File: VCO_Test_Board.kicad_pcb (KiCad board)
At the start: 2 copper layers, 99.1 x 71.1 mm, 19 parts, among them J1 PCB.SMAFRA.HT, J2 PCB.SMAFRA.HT, J3 Tune Voltage Input, J4 VCC, Y1 MAX2607EUT+T

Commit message: Export gerber files.
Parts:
- moved C5 69.3 mm to (95.0, 59.7)
- moved L2 69.0 mm to (48.3, 49.5)
- moved L3 69.0 mm to (54.3, 50.3)
- moved C1 69.0 mm to (54.3, 56.1)
- moved C3 69.0 mm to (77.7, 56.0)
- moved C4 69.0 mm to (95.0, 51.0)
- moved J2 69.0 mm to (109.2, 79.3)
- moved J3 69.0 mm to (40.6, 78.9)
- moved J4 69.0 mm to (111.8, 56.0)
- moved L1 69.0 mm to (51.9, 45.9)
- moved L4 69.0 mm to (66.0, 48.7)
- moved L5 69.0 mm to (66.0, 54.4)
- moved R1 69.0 mm to (44.7, 57.9)
- moved R2 69.0 mm to (69.5, 54.4)
- moved R3 69.0 mm to (69.5, 48.7)
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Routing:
- net GND: track 22.9 -> 20.4 mm
- net Net-(J4-Pin_1): track 21.0 -> 19.0 mm
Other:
- board size 99.1 x 71.1 mm -> 101.6 x 67.7 mm

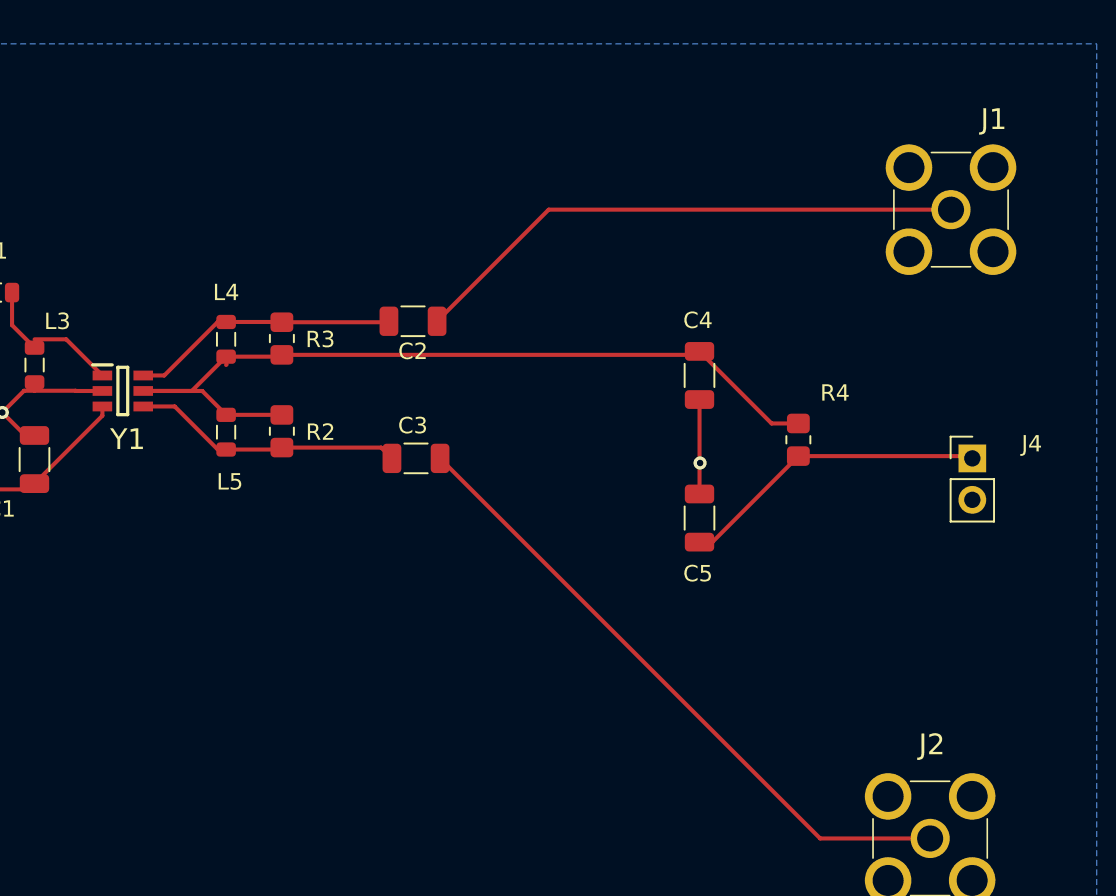
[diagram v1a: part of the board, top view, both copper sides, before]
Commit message: Swap out C5 for Tantalum capacitor. Final export for board order.
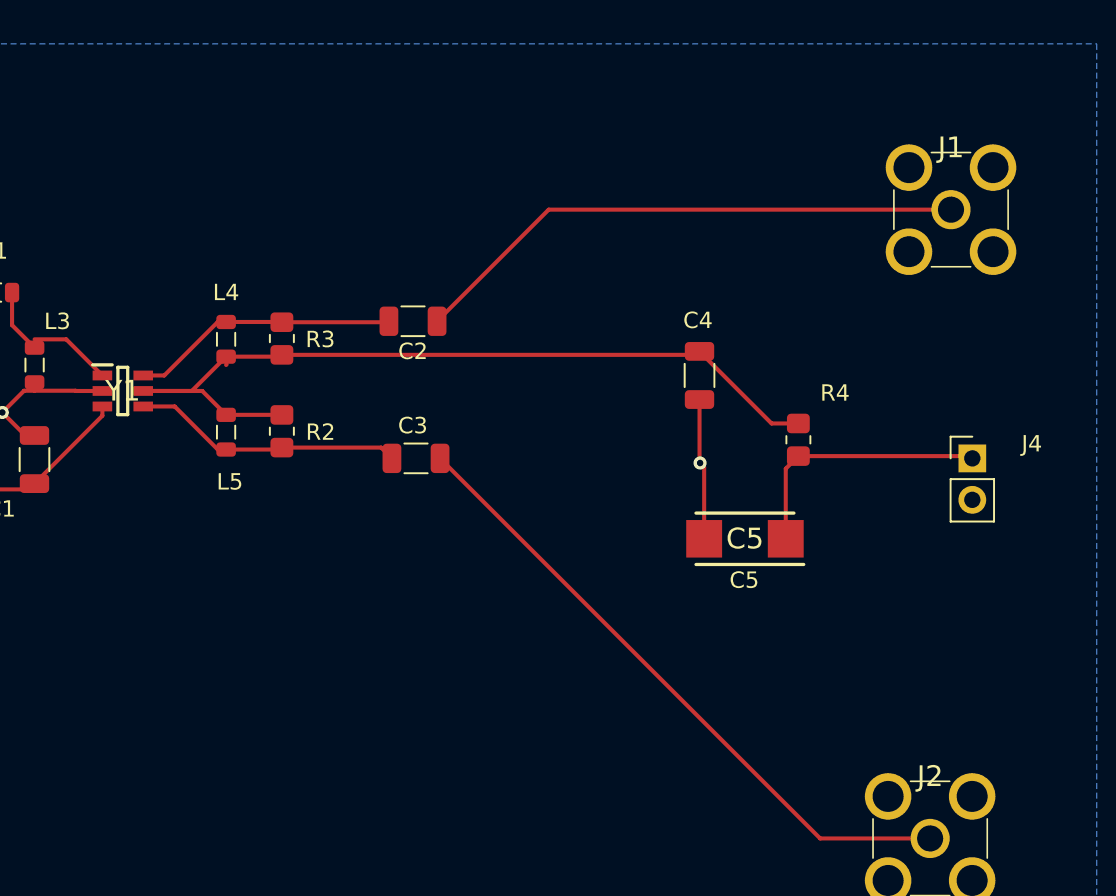
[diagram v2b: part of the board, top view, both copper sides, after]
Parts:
- C5: footprint Capacitor_SMD:C_1206_3216Metric -> Mouser:CAPPM6032X280N
- moved C5 3.06 mm to (97.8, 61.0), turned to 180 degrees
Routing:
- net GND: track 20.4 -> 23.3 mm
- net Net-(C5-+): track 19.0 -> 16.1 mm
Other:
- board text added: "10 uF"
- board text added: "C5"

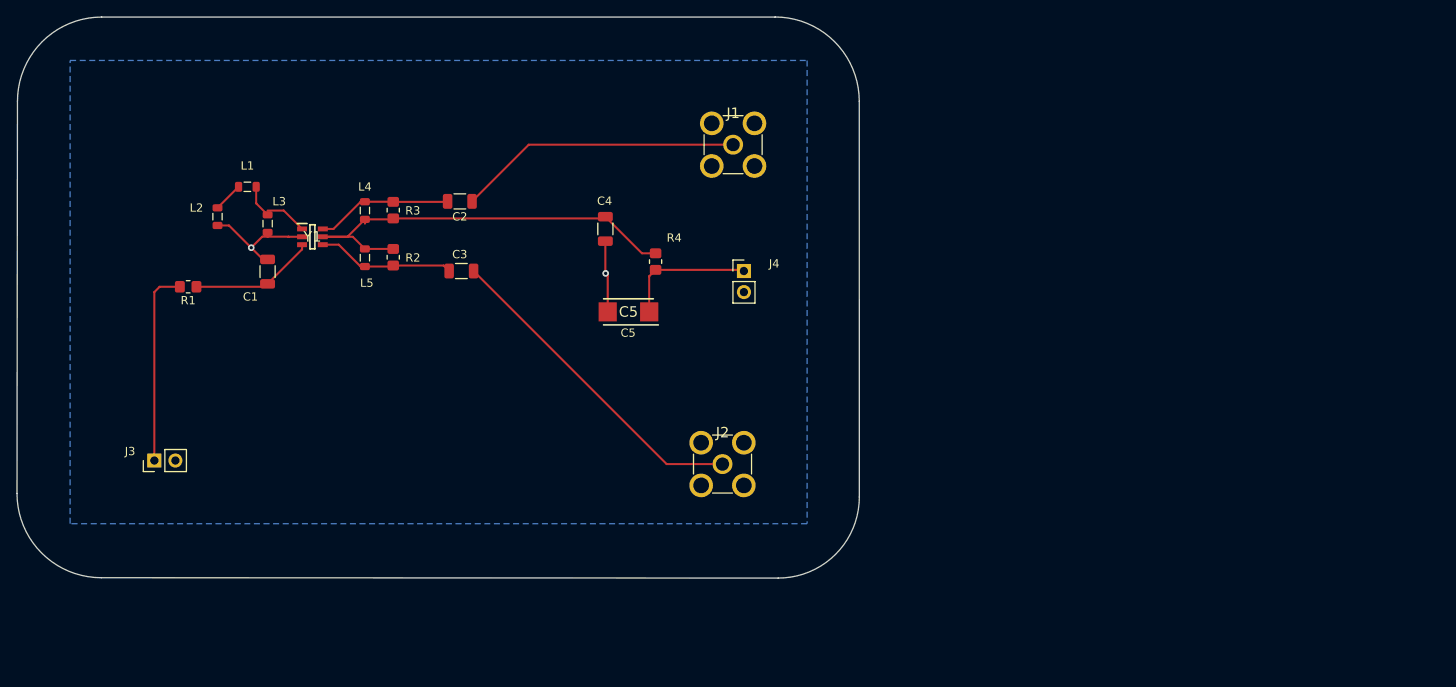
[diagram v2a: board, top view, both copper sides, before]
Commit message: Add mounting holes. Fix silkscreen in a few places.
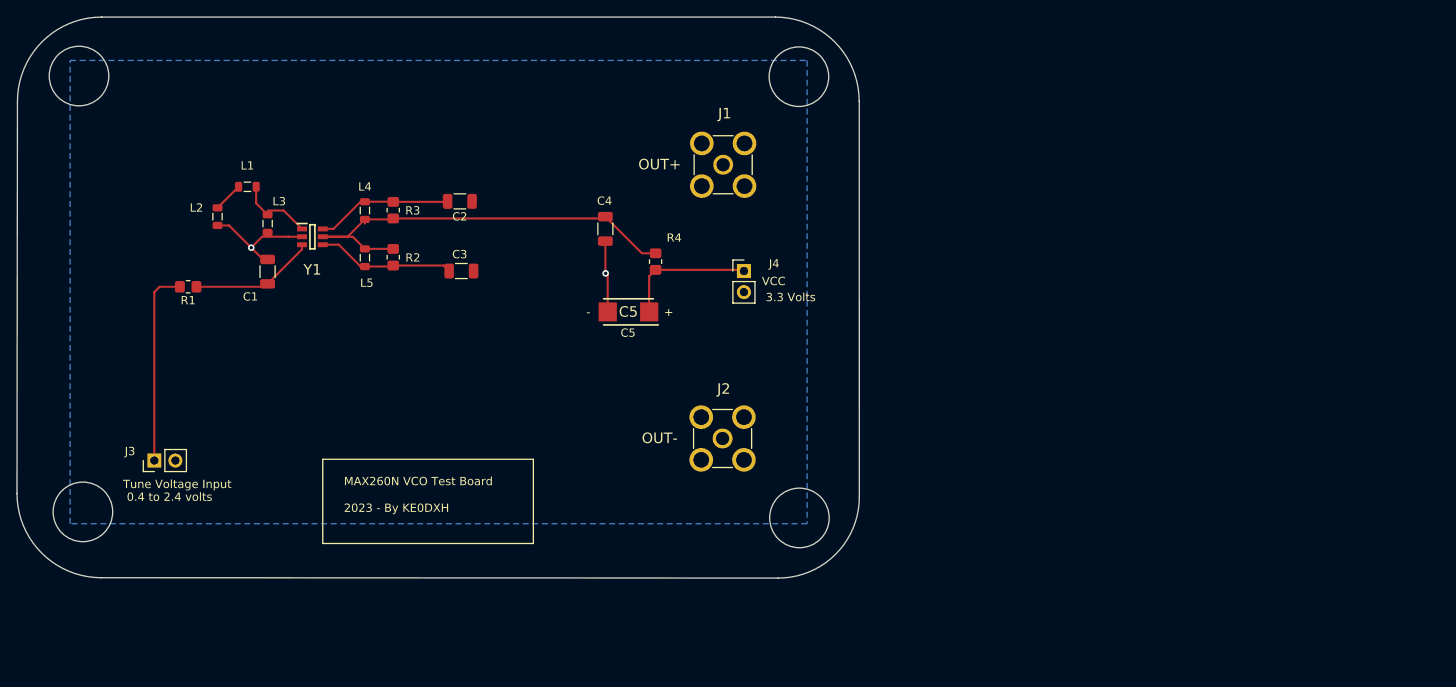
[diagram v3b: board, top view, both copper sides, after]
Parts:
- moved J2 3.09 mm to (109.2, 76.2), turned to -90 degrees
- moved J1 2.70 mm to (109.3, 43.2), turned to -90 degrees
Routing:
- net Net-(C3-Pad1): track 39.7 -> 0.00 mm
- net Net-(C2-Pad1): track 33.1 -> 0.00 mm
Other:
- outline, holes or cut-outs redrawn
- board text added: "+"
- board text added: "-"
- board text added: "MAX260N VCO Test Board 2023 - By KE0DXH"
- board text added: "OUT+"
- board text added: "OUT-"
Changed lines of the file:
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@@
     (property "ki_description" "MAXIM INTEGRATED PRODUCTS - MAX2607EUT+T - VCO, DIFF OUTPUT, 300MHZ, 5.5V, SOT-23")
     (attr smd)
-    (fp_text reference "Y1" (at 0 0) (layer "F.SilkS")
+    (fp_text reference "Y1" (at 0 3.975923) (layer "F.SilkS")
         (effects (font (size 1.27 1.27) (thickness 0.254)))
     )
@@
         (effects (font (size 1 1) (thickness 0.15)))
     )
-    (fp_text value "Tune Voltage Input" (at -2.85678 2.774945) (layer "F.Fab")
+    (fp_text value "Tune Voltage Input" (at -2.85678 2.774945) (layer "F.SilkS")
         (effects (font (size 1 1) (thickness 0.15)))
     )
@@
   )
   (footprint "Mouser:PCBSMAFRAHT" (layer "F.Cu")
-    (at 110.455 40.794077)
+    (at 109.255 43.215 -90)
     (descr "PCB.SMAFRA.HT-2")
     (tags "Connector")
@@
     (property "ki_description" "RF Connectors / Coaxial Connectors SMA RA PCB Mount, Jack, Gold, 50 , Through Hole Pin")
     (attr through_hole)
-    (fp_text reference "J1" (at 0 -3.8) (layer "F.SilkS")
+    (fp_text reference "J1" (at -6.179724 -0.190511) (layer "F.SilkS")
         (effects (font (size 1.27 1.27) (thickness 0.254)))
     )
-    (fp_text value "PCB.SMAFRA.HT" (at 0 -3.8) (layer "F.SilkS") hide
-        (effects (font (size 1.27 1.27) (thickness 0.254)))
-    )
-    (fp_text user "${REFERENCE}" (at 0 -3.8) (layer "F.Fab")
+    (fp_text value "PCB.SMAFRA.HT" (at 0 -3.8 90) (layer "F.SilkS") hide
         (effects (font (size 1.27 1.27) (thickness 0.254)))
     )
@@
     (fp_line (start 3.5 3.5) (end -3.5 3.5)
       (stroke (width 0.2) (type solid)) (layer "F.Fab"))
-    (pad "1" thru_hole circle (at 0 0) (size 2.4 2.4) (drill 1.6) (layers "*.Cu" "*.Mask")
+    (pad "1" thru_hole circle (at 0 0 270) (size 2.4 2.4) (drill 1.6) (layers "*.Cu" "*.Mask")
       (net 3 "Net-(C2-Pad1)") (pinfunction "1") (pintype "passive"))
-    (pad "2" thru_hole circle (at -2.575 -2.575) (size 2.85 2.85) (drill 1.9) (layers "*.Cu" "*.Mask")
+    (pad "2" thru_hole circle (at -2.575 -2.575 270) (size 2.85 2.85) (drill 1.9) (layers "*.Cu" "*.Mask")
       (net 2 "GND") (pinfunction "2") (pintype "passive"))
-    (pad "3" thru_hole circle (at -2.575 2.575) (size 2.85 2.85) (drill 1.9) (layers "*.Cu" "*.Mask")
+    (pad "3" thru_hole circle (at -2.575 2.575 270) (size 2.85 2.85) (drill 1.9) (layers "*.Cu" "*.Mask")
       (net 2 "GND") (pinfunction "3") (pintype "passive"))
-    (pad "4" thru_hole circle (at 2.575 2.575) (size 2.85 2.85) (drill 1.9) (layers "*.Cu" "*.Mask")
+    (pad "4" thru_hole circle (at 2.575 2.575 270) (size 2.85 2.85) (drill 1.9) (layers "*.Cu" "*.Mask")
       (net 2 "GND") (pinfunction "4") (pintype "passive"))
-    (pad "5" thru_hole circle (at 2.575 -2.575) (size 2.85 2.85) (drill 1.9) (layers "*.Cu" "*.Mask")
+    (pad "5" thru_hole circle (at 2.575 -2.575 270) (size 2.85 2.85) (drill 1.9) (layers "*.Cu" "*.Mask")
       (net 2 "GND") (pinfunction "5") (pintype "passive"))
     (model "C:\\Users\\steve\\OneDrive\\Documents\\EDA\\SamacSys_Parts.3dshapes\\PCB.SMAFRA.HT.stp"
@@
         (effects (font (size 1 1) (thickness 0.15)))
     )
-    (fp_text value "VCC" (at 3.594817 1.237918) (layer "F.Fab")
+    (fp_text value "VCC" (at 3.594817 1.237918) (layer "F.SilkS")
         (effects (font (size 1 1) (thickness 0.15)))
     )
@@
   )
   (footprint "Mouser:PCBSMAFRAHT" (layer "F.Cu")
-    (at 109.175699 79.32015)
+    (at 109.185 76.235 -90)
     (descr "PCB.SMAFRA.HT-2")
     (tags "Connector")
@@
     (property "ki_description" "RF Connectors / Coaxial Connectors SMA RA PCB Mount, Jack, Gold, 50 , Through Hole Pin")
     (attr through_hole)
-    (fp_text reference "J2" (at 0 -3.8) (layer "F.SilkS")
+    (fp_text reference "J2" (at -5.975188 -0.144266) (layer "F.SilkS")
         (effects (font (size 1.27 1.27) (thickness 0.254)))
     )
-    (fp_text value "PCB.SMAFRA.HT" (at 0 -3.8) (layer "F.SilkS") hide
-        (effects (font (size 1.27 1.27) (thickness 0.254)))
-    )
-    (fp_text user "${REFERENCE}" (at 0 -3.8) (layer "F.Fab")
+    (fp_text value "PCB.SMAFRA.HT" (at 0 -3.8 90) (layer "F.SilkS") hide
         (effects (font (size 1.27 1.27) (thickness 0.254)))
     )
@@
     (fp_line (start 3.5 3.5) (end -3.5 3.5)
       (stroke (width 0.2) (type solid)) (layer "F.Fab"))
-    (pad "1" thru_hole circle (at 0 0) (size 2.4 2.4) (drill 1.6) (layers "*.Cu" "*.Mask")
+    (pad "1" thru_hole circle (at 0 0 270) (size 2.4 2.4) (drill 1.6) (layers "*.Cu" "*.Mask")
       (net 4 "Net-(C3-Pad1)") (pinfunction "1") (pintype "passive"))
-    (pad "2" thru_hole circle (at -2.575 -2.575) (size 2.85 2.85) (drill 1.9) (layers "*.Cu" "*.Mask")
+    (pad "2" thru_hole circle (at -2.575 -2.575 270) (size 2.85 2.85) (drill 1.9) (layers "*.Cu" "*.Mask")
       (net 2 "GND") (pinfunction "2") (pintype "passive"))
-    (pad "3" thru_hole circle (at -2.575 2.575) (size 2.85 2.85) (drill 1.9) (layers "*.Cu" "*.Mask")
+    (pad "3" thru_hole circle (at -2.575 2.575 270) (size 2.85 2.85) (drill 1.9) (layers "*.Cu" "*.Mask")
       (net 2 "GND") (pinfunction "3") (pintype "passive"))
-    (pad "4" thru_hole circle (at 2.575 2.575) (size 2.85 2.85) (drill 1.9) (layers "*.Cu" "*.Mask")
+    (pad "4" thru_hole circle (at 2.575 2.575 270) (size 2.85 2.85) (drill 1.9) (layers "*.Cu" "*.Mask")
       (net 2 "GND") (pinfunction "4") (pintype "passive"))
-    (pad "5" thru_hole circle (at 2.575 -2.575) (size 2.85 2.85) (drill 1.9) (layers "*.Cu" "*.Mask")
+    (pad "5" thru_hole circle (at 2.575 -2.575 270) (size 2.85 2.85) (drill 1.9) (layers "*.Cu" "*.Mask")
       (net 2 "GND") (pinfunction "5") (pintype "passive"))
     (model "C:\\Users\\steve\\OneDrive\\Documents\\EDA\\SamacSys_Parts.3dshapes\\PCB.SMAFRA.HT.stp"
@@
     )
   )
-  (gr_arc (start 115.510574 25.391716) (mid 122.694779 28.367511) (end 125.670574 35.551716)
+  (gr_rect (start 60.96 78.74) (end 86.36 88.9)
+    (stroke (width 0.15) (type default)) (fill none) (layer "F.SilkS"))
+  (gr_arc (start 115.57 25.400001) (mid 122.710034 28.394279) (end 125.662473 35.551716)
     (stroke (width 0.1) (type default)) (layer "Edge.Cuts"))
   (gr_line (start 34.233463 93.02852) (end 115.89509 93.071952)
@@
   (gr_line (start 125.681091 83.285951) (end 125.670574 35.551716)
     (stroke (width 0.1) (type default)) (layer "Edge.Cuts"))
+  (gr_circle (center 118.393006 32.593365) (end 121.985108 32.593365)
+    (stroke (width 0.15) (type default)) (fill none) (layer "Edge.Cuts"))
   (gr_arc (start 24.13 35.56) (mid 27.105795 28.375795) (end 34.29 25.4)
     (stroke (width 0.1) (type default)) (layer "Edge.Cuts"))
+  (gr_circle (center 31.555692 32.515133) (end 35.147794 32.515133)
+    (stroke (width 0.15) (type default)) (fill none) (layer "Edge.Cuts"))
   (gr_line (start 24.073463 82.86852) (end 24.13 35.56)
     (stroke (width 0.1) (type default)) (layer "Edge.Cuts"))
+  (gr_circle (center 32.025083 85.086912) (end 35.617185 85.086912)
+    (stroke (width 0.15) (type default)) (fill none) (layer "Edge.Cuts"))
   (gr_arc (start 34.233463 93.02852) (mid 27.049258 90.052725) (end 24.073463 82.86852)
     (stroke (width 0.1) (type default)) (layer "Edge.Cuts"))
   (gr_line (start 34.29 25.4) (end 115.57 25.4)
     (stroke (width 0.1) (type default)) (layer "Edge.Cuts"))
+  (gr_circle (center 118.453511 85.815264) (end 122.045613 85.815264)
+    (stroke (width 0.15) (type default)) (fill none) (layer "Edge.Cuts"))
+  (gr_text "OUT+" (at 101.6 43.18) (layer "F.SilkS")
+    (effects (font (size 1.27 1.27) (thickness 0.254)))
+  )
+  (gr_text "3.3 Volts" (at 117.404217 59.206251) (layer "F.SilkS")
+    (effects (font (size 1 1) (thickness 0.15)))
+  )
+  (gr_text "MAX260N VCO Test Board\n\n2023 - By KE0DXH\n\n" (at 63.5 83.82) (layer "F.SilkS")
+    (effects (font (size 1 1) (thickness 0.15)) (justify left))
+  )
+  (gr_text "0.4 to 2.4 volts" (at 42.477964 83.294119) (layer "F.SilkS")
+    (effects (font (size 1 1) (thickness 0.15)))
+  )
   (gr_text "C5" (at 97.79 63.5) (layer "F.SilkS")
     (effects (font (size 1 1) (thickness 0.15)))
   )
-  (gr_text "3.3 Volts" (at 117.404217 59.206251) (layer "F.Fab")
+  (gr_text "OUT-" (at 101.6 76.2) (layer "F.SilkS")
+    (effects (font (size 1.27 1.27) (thickness 0.254)))
+  )
+  (gr_text "+" (at 102.684462 61.004013) (layer "F.SilkS")
     (effects (font (size 1 1) (thickness 0.15)))
   )
-  (gr_text "0.4 to 2.4 volts" (at 42.477964 83.294119) (layer "F.Fab")
+  (gr_text "-" (at 92.986943 60.985819) (layer "F.SilkS")
     (effects (font (size 1 1) (thickness 0.15)))
   )
@@
   (via (at 95.079572 56.317657) (size 0.8) (drill 0.4) (layers "F.Cu" "B.Cu") (free) (net 2))
   (via (at 52.328723 53.221381) (size 0.8) (drill 0.4) (layers "F.Cu" "B.Cu") (free) (net 2))
-  (segment (start 78.966105 47.632526) (end 85.804554 40.794077) (width 0.25) (layer "F.Cu") (net 3))
-  (segment (start 85.804554 40.794077) (end 109.22 40.794077) (width 0.25) (layer "F.Cu") (net 3))
-  (segment (start 79.15 56.034077) (end 102.436073 79.32015) (width 0.25) (layer "F.Cu") (net 4))
-  (segment (start 102.436073 79.32015) (end 109.175699 79.32015) (width 0.25) (layer "F.Cu") (net 4))
   (segment (start 53.946097 57.934077) (end 54.299589 57.580585) (width 0.25) (layer "F.Cu") (net 5))
   (segment (start 45.72 57.934077) (end 53.946097 57.934077) (width 0.25) (layer "F.Cu") (net 5))
@@
     )
   )
-  (group "" (id 96585ef3-8c30-40ad-8ac0-88ff5b5410ec)
-    (members
-      2b9131db-60c4-4bd3-917c-fc71bccf163e
-      3e48a34a-59ec-4646-84b5-7698e987e1a7
-      70b12d8d-1f4b-4498-bade-dfc615c9c443
-      7de7da3b-8ee1-44ad-a89d-f5796a0eff8b
-      97735e73-0923-433e-8450-2501ef96361e
-      a1db13d8-aa48-4faa-ad8d-5f91cbae564e
-      b593c34c-7c93-47e1-b201-1b2a8035dfaa
-      d86577f8-7886-429a-b139-4c4b0027cead
-    )
-  )
